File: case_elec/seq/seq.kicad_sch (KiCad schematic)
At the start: 16 parts, among them J1 LiPo BMS, J10 Alim secours, J11 Coupleur, J12 Jack, J2 Lipo Alim, J3 B+, J4 BM, J5 B-, J6 P+, J7 P-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

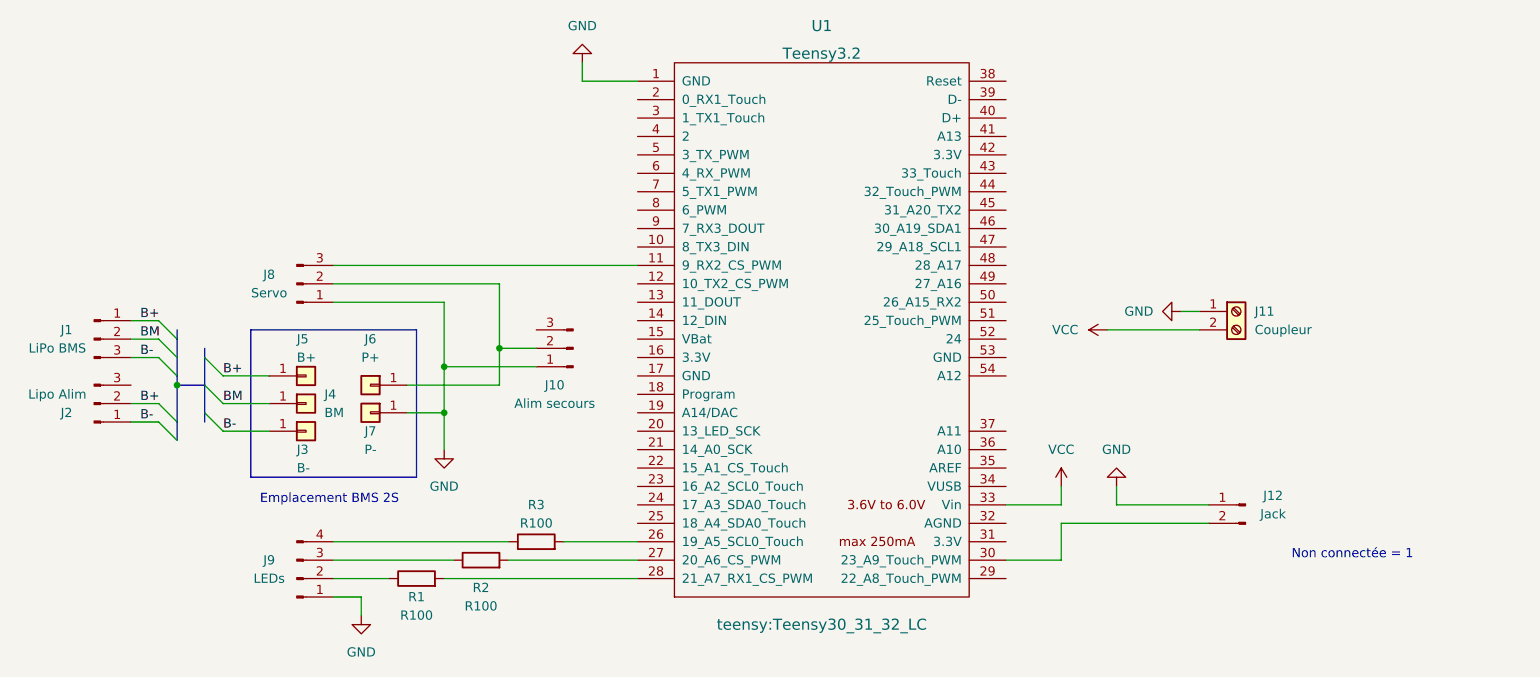
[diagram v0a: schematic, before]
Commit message: solution finale utilisée en vol
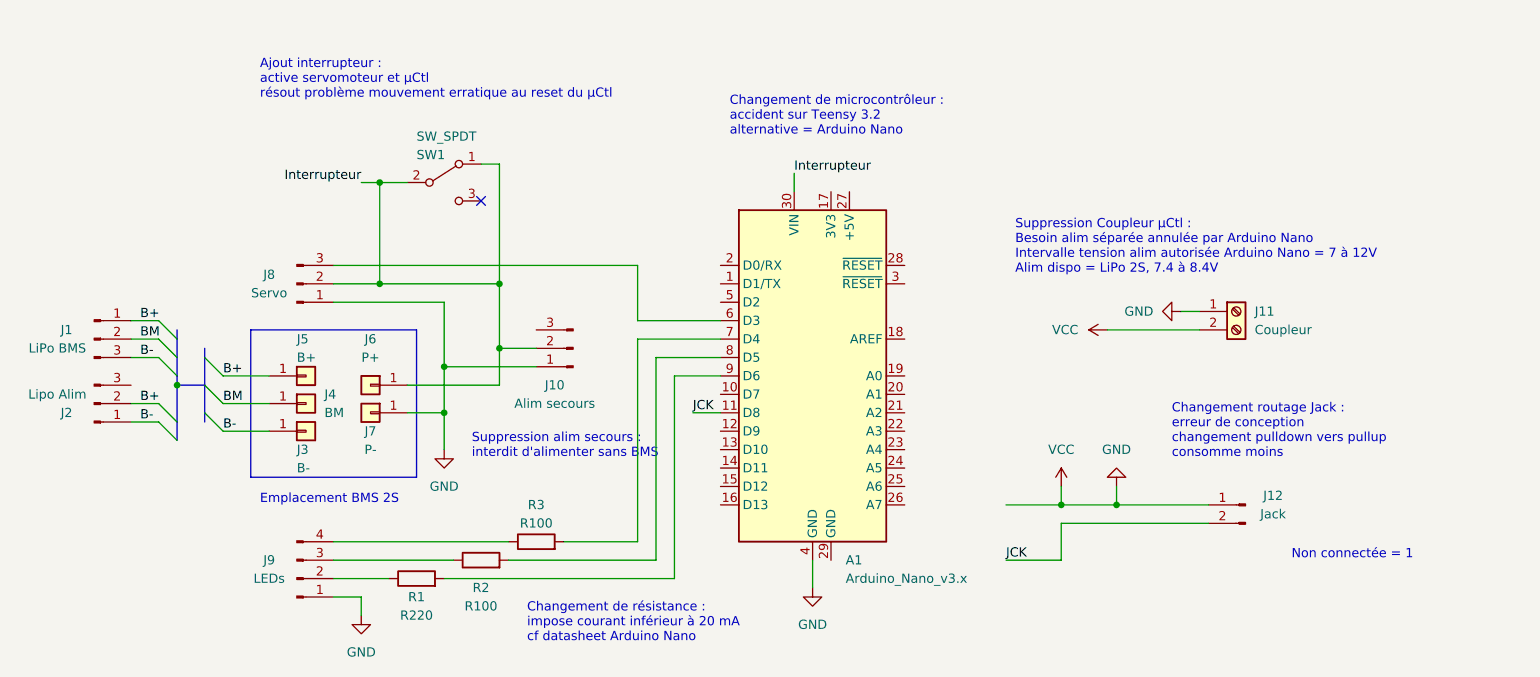
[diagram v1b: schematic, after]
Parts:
- removed U1: Teensy3.2, teensy:Teensy30_31_32_LC, symbol teensy:Teensy3.2
- added A1: Arduino_Nano_v3.x, Module:Arduino_Nano, symbol MCU_Module:Arduino_Nano_v3.x
- added SW1: SW_SPDT, symbol Switch:SW_SPDT
- R1: value R100 -> R220
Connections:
- net VCC is gone; now on net GND: J11.2 (Pin_2)
- net GND: now also A1.4 (GND)
- net at R1.2: now also A1.9 (D6)
- net JCK: now reaches J12.2 (Pin_2)
- net JCK: now also A1.11 (D8)
- net Interrupteur: now reaches J10.2 (Pin_2), J6.1 (Pin_1), J8.2 (Pin_2)
- net Interrupteur: now also A1.30 (VIN), SW1.1 (A), SW1.2 (B)
- net at J8.3 (Pin_3): now also A1.6 (D3)
- net at R3.2: now also A1.7 (D4)
- net at R2.2: now also A1.8 (D5)
- no-connect marks 0 -> 1
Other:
- note added: "Ajout interrupteur : active servomoteur et µCtl résout problème mouvement erratique au reset du µCtl"
- note added: "Changement de microcontrôleur : accident sur Teensy 3.2 alternative = Arduino Nano"
- note added: "Changement de résistance : impose courant inférieur à 20 mA cf datasheet Arduino Nano"
- note added: "Changement routage Jack : erreur de conception changement pulldown vers pullup consomme moins"
- note added: "Suppression Coupleur µCtl : Besoin alim séparée annulée par Arduino Nano Intervalle tension alim autorisée Arduino Nano = 7 à 12V Alim dispo = LiPo 2S, 7.4 à 8.4V"
- note added: "Suppression alim secours : interdit d'alimenter sans BMS"
